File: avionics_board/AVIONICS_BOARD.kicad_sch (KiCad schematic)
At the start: 17 parts

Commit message: EPS AVI SCI SCIwoSwitches RF AUX all updated to use RNs. BOMs completed
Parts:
- RN1, RN2: Manufacturer (none) -> Panasonic; Part Number (none) -> EXB-24V220JX; Tolerance (none) -> 5
- RN3, RN4, RN5: Manufacturer (none) -> Panasonic; Part Number (none) -> EXB-24V562JX; Tolerance (none) -> 5
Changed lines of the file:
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@@
 			)
 		)
-		(property "Datasheet" "~"
+		(property "Datasheet" "https://industrial.panasonic.com/cdbs/www-data/pdf/AOC0000/AOC0000C14.pdf"
 			(at 85.725 101.6 0)
 			(effects
@@
 			)
 		)
-		(property "Manufactorer" ""
+		(property "Manufacturer" "Panasonic"
 			(at 85.725 101.6 0)
 			(effects
@@
 					(size 1.27 1.27)
 				)
-			)
-		)
-		(property "Sim.Pins" ""
+				(hide yes)
+			)
+		)
+		(property "Part Number" "EXB-24V562JX"
 			(at 85.725 101.6 0)
 			(effects
@@
 					(size 1.27 1.27)
 				)
+				(hide yes)
+			)
+		)
+		(property "Tolerance" "5"
+			(at 85.725 101.6 0)
+			(effects
+				(font
+					(size 1.27 1.27)
+				)
+				(hide yes)
 			)
 		)
@@
 				)
 				(hide yes)
-			)
-		)
-		(property "Manufactorer" ""
-			(at 243.205 159.385 0)
-			(effects
-				(font
-					(size 1.27 1.27)
-				)
-			)
-		)
-		(property "Sim.Pins" ""
-			(at 243.205 159.385 0)
-			(effects
-				(font
-					(size 1.27 1.27)
-				)
 			)
 		)
@@
 			)
 		)
-		(property "Manufactorer" ""
-			(at 243.205 154.305 0)
-			(effects
-				(font
-					(size 1.27 1.27)
-				)
-			)
-		)
-		(property "Sim.Pins" ""
-			(at 243.205 154.305 0)
-			(effects
-				(font
-					(size 1.27 1.27)
-				)
-			)
-		)
 		(pin "1"
 		)
@@
 			)
 		)
-		(property "Datasheet" "~"
+		(property "Datasheet" "https://industrial.panasonic.com/cdbs/www-data/pdf/AOC0000/AOC0000C14.pdf"
 			(at 91.44 78.105 0)
 			(effects
@@
 			)
 		)
-		(property "Manufactorer" ""
-			(at 91.44 78.105 0)
-			(effects
-				(font
-					(size 1.27 1.27)
-				)
-			)
-		)
-		(property "Sim.Pins" ""
-			(at 91.44 78.105 0)
-			(effects
-				(font
-					(size 1.27 1.27)
-				)
+		(property "Manufacturer" "Panasonic"
+			(at 91.44 78.105 90)
+			(effects
+				(font
+					(size 1.27 1.27)
+				)
+				(hide yes)
+			)
+		)
+		(property "Part Number" "EXB-24V220JX"
+			(at 91.44 78.105 90)
+			(effects
+				(font
+					(size 1.27 1.27)
+				)
+				(hide yes)
+			)
+		)
+		(property "Tolerance" "5"
+			(at 91.44 78.105 90)
+			(effects
+				(font
+					(size 1.27 1.27)
+				)
+				(hide yes)
 			)
 		)
@@
 			)
 		)
-		(property "Datasheet" "~"
+		(property "Datasheet" "https://industrial.panasonic.com/cdbs/www-data/pdf/AOC0000/AOC0000C14.pdf"
 			(at 57.785 196.215 0)
 			(effects
@@
 			)
 		)
-		(property "Manufactorer" ""
+		(property "Manufacturer" "Panasonic"
 			(at 57.785 196.215 0)
 			(effects
@@
 					(size 1.27 1.27)
 				)
-			)
-		)
-		(property "Sim.Pins" ""
+				(hide yes)
+			)
+		)
+		(property "Part Number" "EXB-24V562JX"
 			(at 57.785 196.215 0)
 			(effects
@@
 					(size 1.27 1.27)
 				)
+				(hide yes)
+			)
+		)
+		(property "Tolerance" "5"
+			(at 57.785 196.215 0)
+			(effects
+				(font
+					(size 1.27 1.27)
+				)
+				(hide yes)
 			)
 		)
@@
 			)
 		)
-		(property "Datasheet" "~"
+		(property "Datasheet" "https://industrial.panasonic.com/cdbs/www-data/pdf/AOC0000/AOC0000C14.pdf"
 			(at 90.17 26.67 0)
 			(effects
@@
 			)
 		)
-		(property "Manufactorer" ""
-			(at 90.17 26.67 0)
-			(effects
-				(font
-					(size 1.27 1.27)
-				)
-			)
-		)
-		(property "Sim.Pins" ""
-			(at 90.17 26.67 0)
-			(effects
-				(font
-					(size 1.27 1.27)
-				)
+		(property "Manufacturer" "Panasonic"
+			(at 90.17 26.67 90)
+			(effects
+				(font
+					(size 1.27 1.27)
+				)
+				(hide yes)
+			)
+		)
+		(property "Part Number" "EXB-24V220JX"
+			(at 90.17 26.67 90)
+			(effects
+				(font
+					(size 1.27 1.27)
+				)
+				(hide yes)
+			)
+		)
+		(property "Tolerance" "5"
+			(at 90.17 26.67 90)
+			(effects
+				(font
+					(size 1.27 1.27)
+				)
+				(hide yes)
 			)
 		)
@@
 			)
 		)
-		(property "Manufactorer" ""
-			(at 243.205 164.465 0)
-			(effects
-				(font
-					(size 1.27 1.27)
-				)
-			)
-		)
-		(property "Sim.Pins" ""
-			(at 243.205 164.465 0)
-			(effects
-				(font
-					(size 1.27 1.27)
-				)
-			)
-		)
 		(pin "1"
 		)
@@
 				)
 				(hide yes)
-			)
-		)
-		(property "Manufactorer" ""
-			(at 184.15 38.1 0)
-			(effects
-				(font
-					(size 1.27 1.27)
-				)
-			)
-		)
-		(property "Sim.Pins" ""
-			(at 184.15 38.1 0)
-			(effects
-				(font
-					(size 1.27 1.27)
-				)
 			)
 		)
@@
 			)
 		)
-		(property "Datasheet" "~"
+		(property "Datasheet" "https://industrial.panasonic.com/cdbs/www-data/pdf/AOC0000/AOC0000C14.pdf"
 			(at 198.12 95.25 0)
 			(effects
@@
 			)
 		)
-		(property "Manufactorer" ""
+		(property "Manufacturer" "Panasonic"
 			(at 198.12 95.25 0)
 			(effects
@@
 					(size 1.27 1.27)
 				)
-			)
-		)
-		(property "Sim.Pins" ""
+				(hide yes)
+			)
+		)
+		(property "Part Number" "EXB-24V562JX"
 			(at 198.12 95.25 0)
 			(effects
@@
 					(size 1.27 1.27)
 				)
+				(hide yes)
+			)
+		)
+		(property "Tolerance" "5"
+			(at 198.12 95.25 0)
+			(effects
+				(font
+					(size 1.27 1.27)
+				)
+				(hide yes)
 			)
 		)
@@
 			)
 		)
-		(property "Manufactorer" ""
-			(at 153.035 38.1 0)
-			(effects
-				(font
-					(size 1.27 1.27)
-				)
-			)
-		)
-		(property "Sim.Pins" ""
-			(at 153.035 38.1 0)
-			(effects
-				(font
-					(size 1.27 1.27)
-				)
-			)
-		)
 		(pin "1"
 		)
@@
 			)
 		)
-		(property "Manufactorer" ""
-			(at 91.44 74.93 0)
-			(effects
-				(font
-					(size 1.27 1.27)
-				)
-			)
-		)
-		(property "Sim.Pins" ""
-			(at 91.44 74.93 0)
-			(effects
-				(font
-					(size 1.27 1.27)
-				)
-			)
-		)
 		(pin "1"
 		)
@@
 				)
 				(hide yes)
-			)
-		)
-		(property "Manufactorer" ""
-			(at 171.45 38.1 0)
-			(effects
-				(font
-					(size 1.27 1.27)
-				)
-			)
-		)
-		(property "Sim.Pins" ""
-			(at 171.45 38.1 0)
-			(effects
-				(font
-					(size 1.27 1.27)
-				)
 			)
 		)
@@
 			)
 		)
-		(property "Manufactorer" ""
-			(at 158.75 38.1 0)
-			(effects
-				(font
-					(size 1.27 1.27)
-				)
-			)
-		)
-		(property "Sim.Pins" ""
-			(at 158.75 38.1 0)
-			(effects
-				(font
-					(size 1.27 1.27)
-				)
-			)
-		)
 		(pin "1"
 		)
@@
 			)
 		)
-		(property "Manufactorer" ""
-			(at 90.17 29.21 0)
-			(effects
-				(font
-					(size 1.27 1.27)
-				)
-			)
-		)
-		(property "Sim.Pins" ""
-			(at 90.17 29.21 0)
-			(effects
-				(font
-					(size 1.27 1.27)
-				)
-			)
-		)
 		(pin "1"
 		)
@@
 			)
 		)
-		(property "Manufactorer" ""
-			(at 177.8 38.1 0)
-			(effects
-				(font
-					(size 1.27 1.27)
-				)
-			)
-		)
-		(property "Sim.Pins" ""
-			(at 177.8 38.1 0)
-			(effects
-				(font
-					(size 1.27 1.27)
-				)
-			)
-		)
 		(pin "1"
 		)
@@
 			)
 		)
-		(property "Manufactorer" ""
-			(at 165.1 38.1 0)
-			(effects
-				(font
-					(size 1.27 1.27)
-				)
-			)
-		)
-		(property "Sim.Pins" ""
-			(at 165.1 38.1 0)
-			(effects
-				(font
-					(size 1.27 1.27)
-				)
-			)
-		)
 		(pin "1"
 		)
@@
 			)
 		)
-		(property "Manufactorer" ""
-			(at 243.205 149.225 0)
-			(effects
-				(font
-					(size 1.27 1.27)
-				)
-			)
-		)
-		(property "Sim.Pins" ""
-			(at 243.205 149.225 0)
-			(effects
-				(font
-					(size 1.27 1.27)
-				)
-			)
-		)

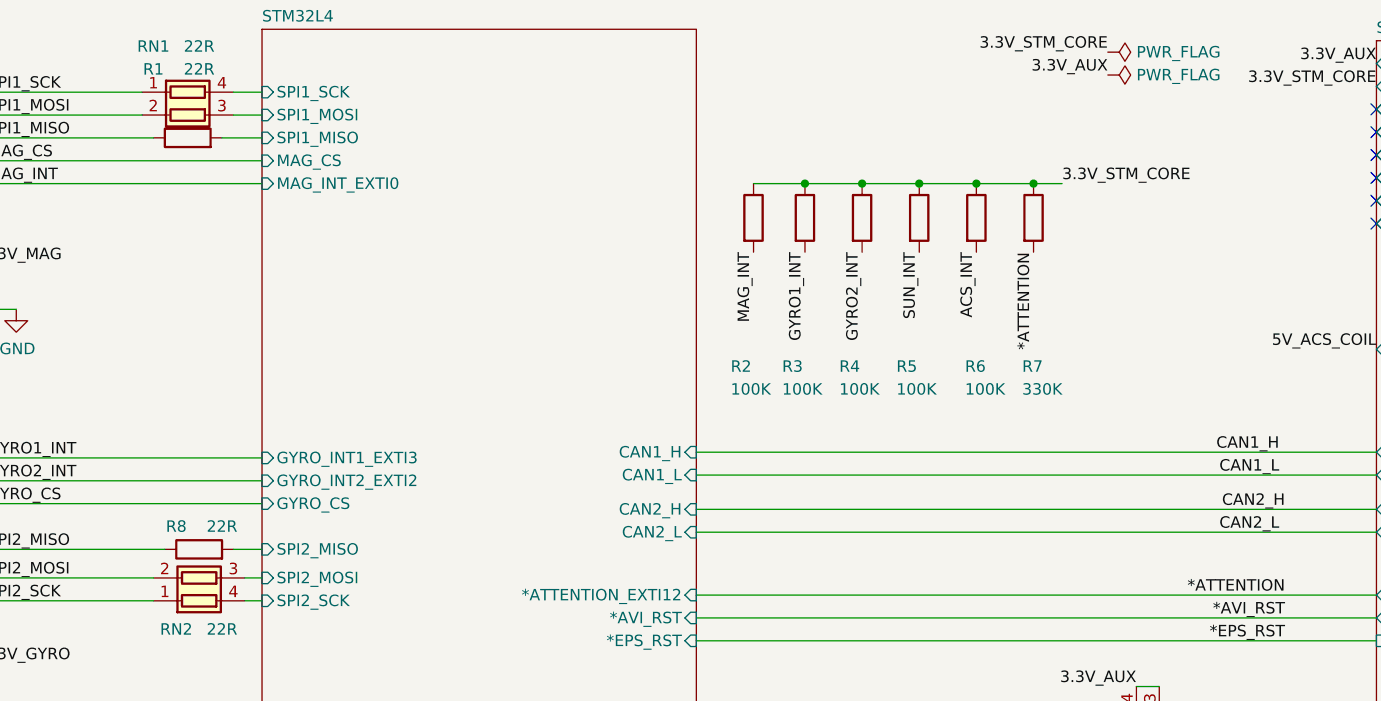
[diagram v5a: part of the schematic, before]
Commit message: sorting out pullups on resets and attention. replace reset with RN where possible. Introduce CN to save some parts
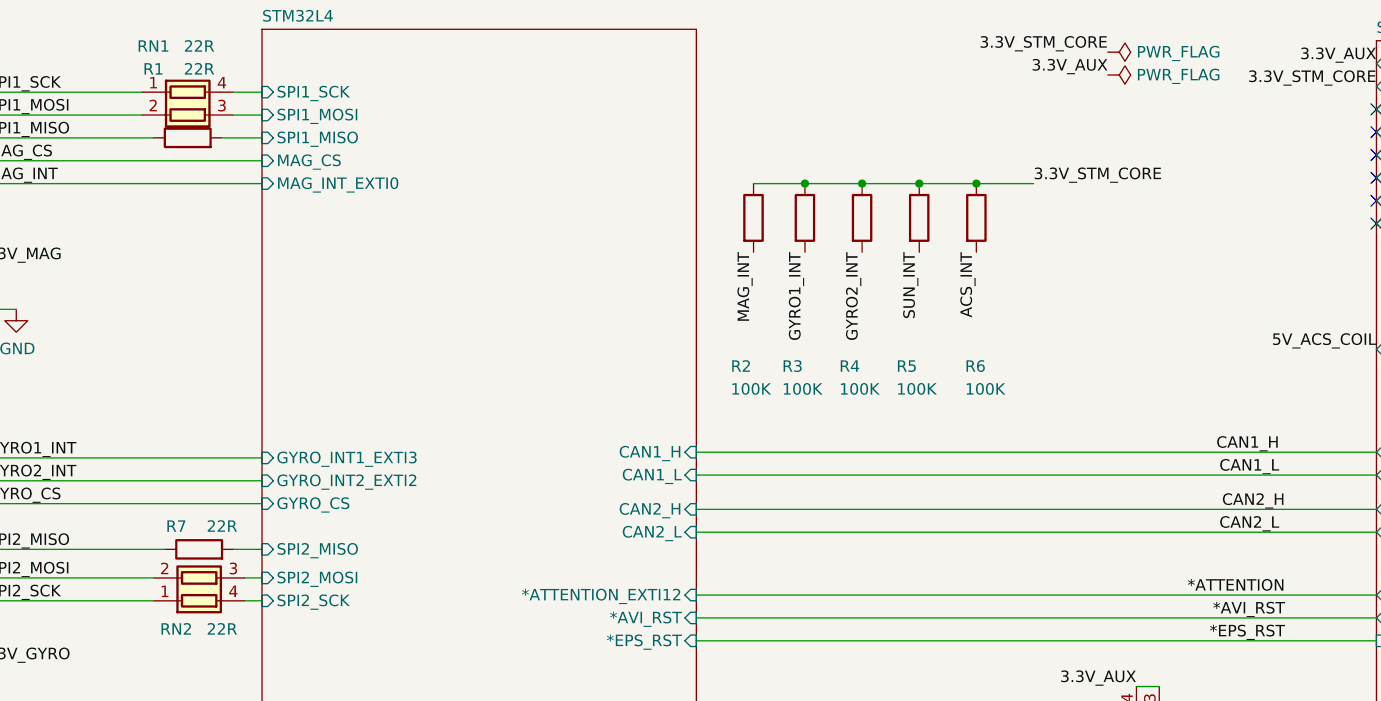
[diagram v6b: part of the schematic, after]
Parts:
- removed R7: 330K, Resistor_SMD:R_0402_1005Metric_Pad0.72x0.64mm_HandSolder, symbol Device:R
- renumbered R8 to R7
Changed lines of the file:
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@@
 	)
 	(junction
-		(at 184.15 34.29)
-		(diameter 0)
-		(color 0 0 0 0)
-	)
-	(junction
 		(at 203.835 133.985)
 		(diameter 0)
@@
 	(wire
 		(pts
-			(xy 187.325 34.29) (xy 184.15 34.29)
-		)
-		(stroke
-			(width 0)
-			(type default)
-		)
-	)
-	(wire
-		(pts
 			(xy 232.41 133.985) (xy 232.41 135.89)
 		)
@@
 	)
 	(label "3.3V_STM_CORE"
-		(at 187.325 34.29 0)
+		(at 184.15 34.29 0)
 		(effects
 			(font
@@
 		)
 	)
-	(label "*ATTENTION"
-		(at 184.15 41.91 270)
-		(effects
-			(font
-				(size 1.27 1.27)
-			)
-			(justify right bottom)
-		)
-	)
 	(label "RST_SUN"
 		(at 69.85 120.65 0)
@@
 	)
 	(symbol
-		(lib_id "Device:R")
-		(at 184.15 38.1 0)
-		(unit 1)
-		(exclude_from_sim no)
-		(in_bom yes)
-		(on_board yes)
-		(dnp no)
-		(property "Reference" "R7"
-			(at 182.88 54.61 0)
-			(effects
-				(font
-					(size 1.27 1.27)
-				)
-				(justify left)
-			)
-		)
-		(property "Value" "330K"
-			(at 182.88 57.15 0)
-			(effects
-				(font
-					(size 1.27 1.27)
-				)
-				(justify left)
-			)
-		)
-		(property "Footprint" "Resistor_SMD:R_0402_1005Metric_Pad0.72x0.64mm_HandSolder"
-			(at 182.372 38.1 90)
-			(effects
-				(font
-					(size 1.27 1.27)
-				)
-				(hide yes)
-			)
-		)
-		(property "Datasheet" "https://www.yageo.com/upload/media/product/products/datasheet/rchip/PYu-RC_Group_51_RoHS_L_12.pdf"
-			(at 184.15 38.1 0)
-			(effects
-				(font
-					(size 1.27 1.27)
-				)
-				(hide yes)
-			)
-		)
-		(property "Description" "Resistor"
-			(at 184.15 38.1 0)
-			(effects
-				(font
-					(size 1.27 1.27)
-				)
-				(hide yes)
-			)
-		)
-		(property "Alt" ""
-			(at 184.15 38.1 0)
-			(effects
-				(font
-					(size 1.27 1.27)
-				)
-				(hide yes)
-			)
-		)
-		(property "Manufacturer" "YAGEO"
-			(at 184.15 38.1 0)
-			(effects
-				(font
-					(size 1.27 1.27)
-				)
-				(hide yes)
-			)
-		)
-		(property "Part Number" "RC0402FR-07330KL"
-			(at 184.15 38.1 0)
-			(effects
-				(font
-					(size 1.27 1.27)
-				)
-				(hide yes)
-			)
-		)
-		(property "Tolerance" "1"
-			(at 184.15 38.1 0)
-			(effects
-				(font
-					(size 1.27 1.27)
-				)
-				(hide yes)
-			)
-		)
-		(pin "1"
-		)
-		(pin "2"
-		)
-		(instances
-			(project "AVIONICS_BOARD"
-				(path "/f6cc00ab-17f1-4973-862f-7ac95fe70668"
-					(reference "R7")
-					(unit 1)
-				)
-			)
-		)
-	)
-	(symbol
 		(lib_id "AVIONICS_BOARD-rescue:GND-power")
 		(at 93.98 198.12 0)
@@
 		(on_board yes)
 		(dnp no)
-		(property "Reference" "R8"
+		(property "Reference" "R7"
 			(at 88.9 72.39 90)
 			(effects
@@
 			(project "AVIONICS_BOARD"
 				(path "/f6cc00ab-17f1-4973-862f-7ac95fe70668"
-					(reference "R8")
+					(reference "R7")
 					(unit 1)
 				)

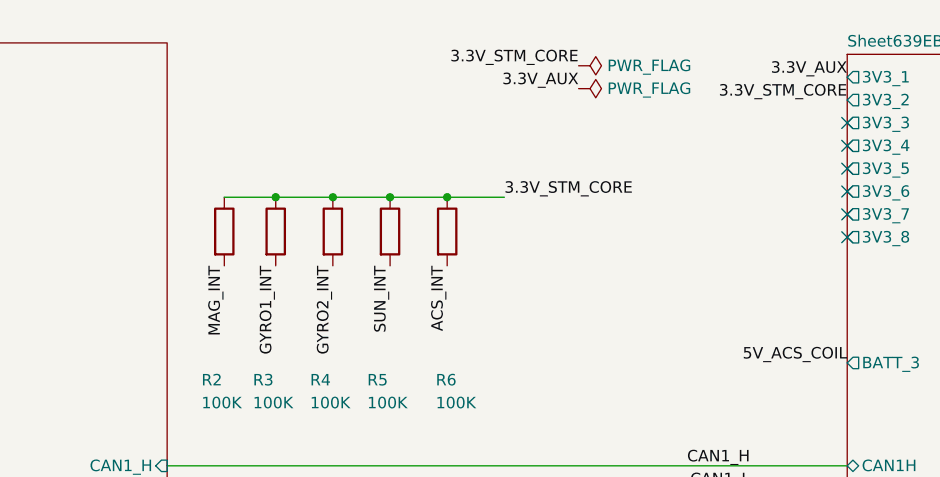
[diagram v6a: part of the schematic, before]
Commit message: cleanup pullups for reset and schmitt trigger for reset; select available thermal NTCs for avi board and use chip for voltage dividers
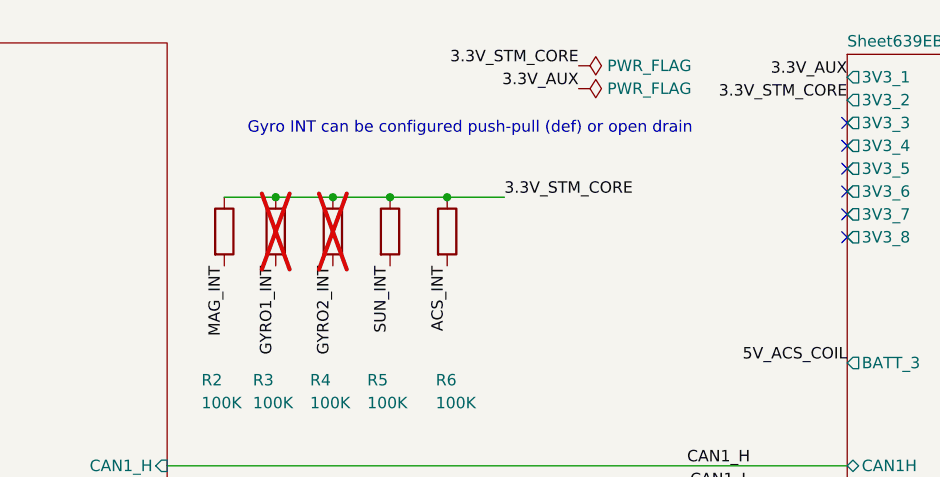
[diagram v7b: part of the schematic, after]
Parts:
- R3, R4: now not fitted
- RN1, RN2, RN3, RN4, RN5: footprint Resistor_SMD:R_Array_Convex_2x0402 -> Common:R_Array_Convex_2x0402_widepads
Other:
- note added: "Gyro INT can be configured push-pull (def) or open drain"
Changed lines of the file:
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@@
 		)
 	)
+	(text "Gyro INT can be configured push-pull (def) or open drain"
+		(exclude_from_sim no)
+		(at 180.34 26.67 0)
+		(effects
+			(font
+				(size 1.27 1.27)
+			)
+		)
+	)
 	(text "ACS\nATTITUDE \nCONTROL \nSUBSYSTEM"
 		(exclude_from_sim no)
@@
 			)
 		)
-		(property "Footprint" "Resistor_SMD:R_Array_Convex_2x0402"
+		(property "Footprint" "Common:R_Array_Convex_2x0402_widepads"
 			(at 90.17 101.6 90)
 			(effects
@@
 			)
 		)
-		(property "Footprint" "Resistor_SMD:R_Array_Convex_2x0402"
+		(property "Footprint" "Common:R_Array_Convex_2x0402_widepads"
 			(at 91.44 73.66 90)
 			(effects
@@
 			)
 		)
-		(property "Footprint" "Resistor_SMD:R_Array_Convex_2x0402"
+		(property "Footprint" "Common:R_Array_Convex_2x0402_widepads"
 			(at 62.23 196.215 90)
 			(effects
@@
 			)
 		)
-		(property "Footprint" "Resistor_SMD:R_Array_Convex_2x0402"
+		(property "Footprint" "Common:R_Array_Convex_2x0402_widepads"
 			(at 90.17 31.115 90)
 			(effects
@@
 			)
 		)
-		(property "Footprint" "Resistor_SMD:R_Array_Convex_2x0402"
+		(property "Footprint" "Common:R_Array_Convex_2x0402_widepads"
 			(at 202.565 95.25 90)
 			(effects
@@
 		(in_bom yes)
 		(on_board yes)
-		(dnp no)
+		(dnp yes)
 		(property "Reference" "R3"
 			(at 156.21 54.61 0)
@@
 		(in_bom yes)
 		(on_board yes)
-		(dnp no)
+		(dnp yes)
 		(property "Reference" "R4"
 			(at 162.56 54.61 0)

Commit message: checked BOM for sci wo switches
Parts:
- added RN2: 100K, Common:R_Array_Convex_2x0402_widepads, symbol Device:R_Pack02
- R2, R5: now not fitted
- R6: value 100K -> 330K; Part Number RC0402FR-07100KL -> RC0402FR-07330KL
- renumbered RN2 to RN3, RN3 to RN4, RN4 to RN5, RN5 to RN6
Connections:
- net *ATTENTION: now also R6.2
- net 3.3V_STM_CORE: now also RN2.3 (R2.2), RN2.4 (R1.2)
- net ACS_INT: now also RN2.2 (R2.1); no longer R6.2
- net SUN_INT: now also RN2.1 (R1.1); no longer R5.2
- new net GYROAUX_INT: R5.2
- no-connect marks 27 -> 26
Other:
- sheet GYRO ports: added INT3; removed none
- sheet STM32L4 ports: added POWER_INT_EXTI7; removed EXTI7
- note added: "Gyro INT can be configured push-pull (def) or open drain Mag INT is push pull"
- note removed: "Gyro INT can be configured push-pull (def) or open drain"
- moved on the sheet: R7, RN3
